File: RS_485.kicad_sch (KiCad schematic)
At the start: 17 parts, among them U6 SP3071EEN-L/TR

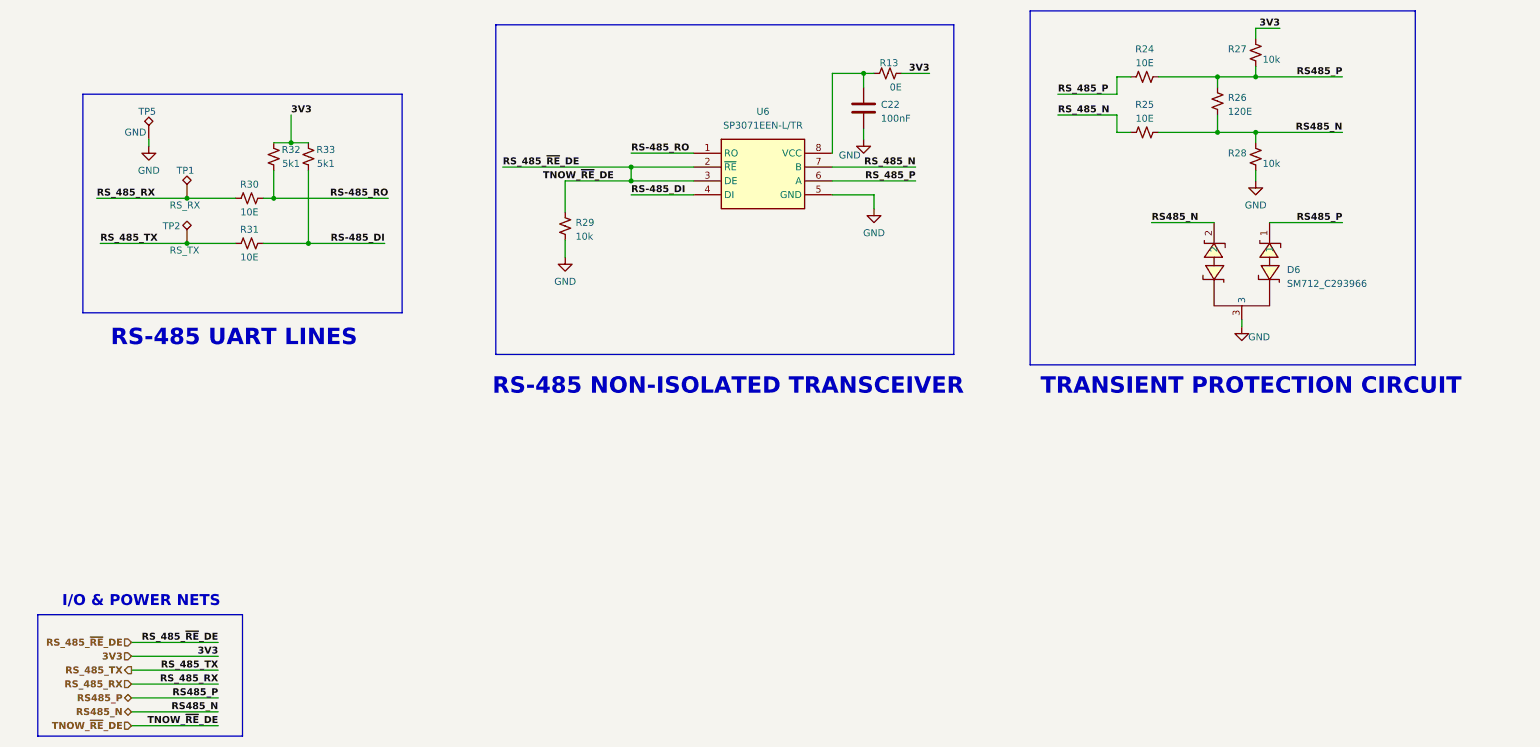
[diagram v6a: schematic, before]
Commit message: Changed GPIO mapping
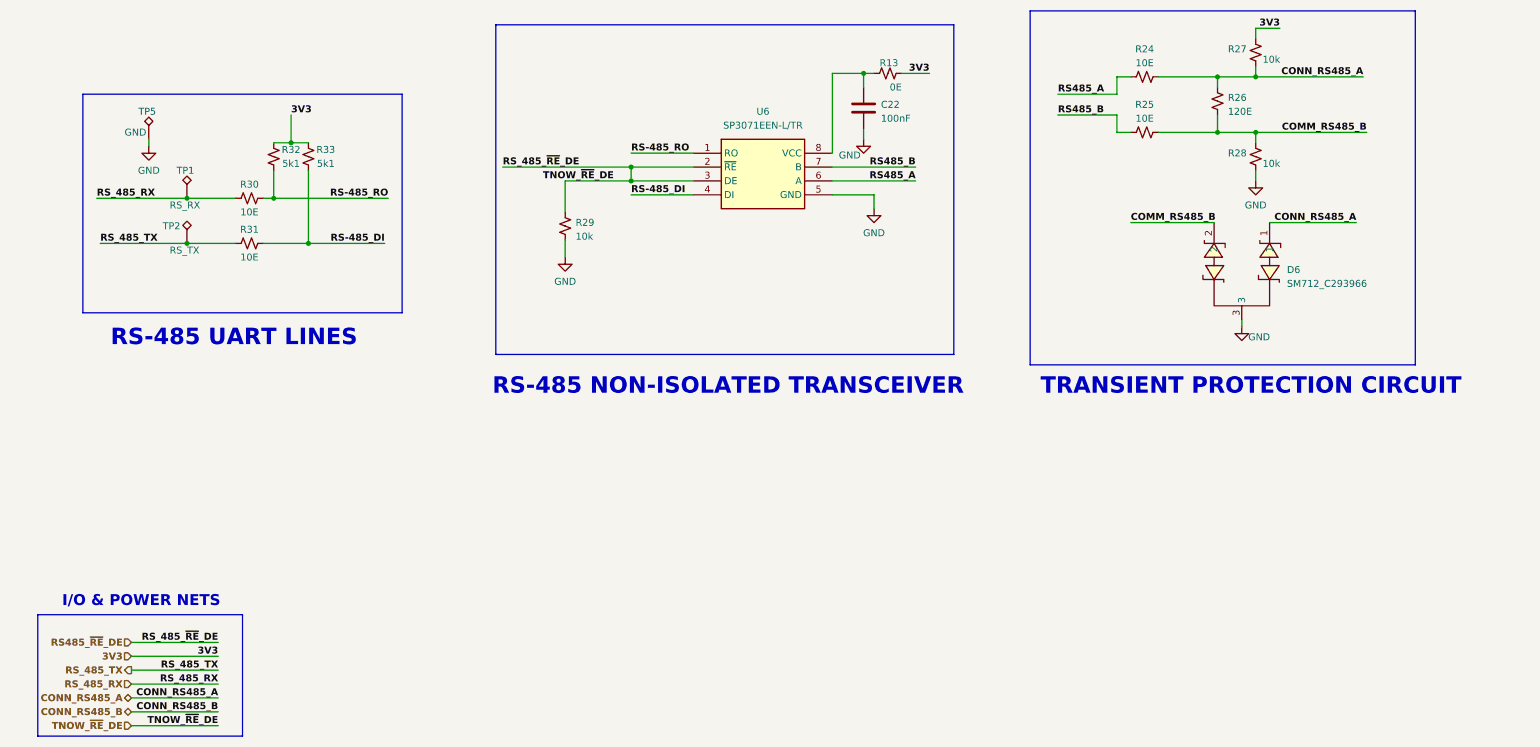
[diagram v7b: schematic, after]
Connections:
- net RS485_N renamed COMM_RS485_B
- net RS485_P renamed CONN_RS485_A
- net RS_485_N renamed RS485_B
- net RS_485_P renamed RS485_A
- net RS_485_~{RE}_DE renamed RS485_~{RE}_DE
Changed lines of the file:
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@@
     (stroke (width 0) (type default))
   )
-  (wire (pts (xy 234.95 97.79) (xy 223.52 97.79))
+  (wire (pts (xy 234.95 97.79) (xy 219.71 97.79))
     (stroke (width 0) (type default))
   )
@@
     (stroke (width 0) (type default))
   )
-  (wire (pts (xy 242.57 81.28) (xy 258.445 81.28))
+  (wire (pts (xy 242.57 81.28) (xy 262.89 81.28))
     (stroke (width 0) (type default))
   )
@@
     (stroke (width 0) (type default))
   )
-  (wire (pts (xy 242.57 71.12) (xy 258.445 71.12))
+  (wire (pts (xy 242.57 71.12) (xy 262.255 71.12))
     (stroke (width 0) (type default))
   )
@@
     (stroke (width 0.5) (type default) (color 0 0 0 1))
   )
-  (wire (pts (xy 258.445 97.79) (xy 245.11 97.79))
+  (wire (pts (xy 260.985 97.79) (xy 245.11 97.79))
     (stroke (width 0) (type default))
   )
@@
     (effects (font (size 3 3) bold (color 255 0 0 1)) (justify left bottom))
   )
-  (label "RS485_P" (at 258.445 97.79 180) (fields_autoplaced)
-    (effects (font (size 1.27 1.27) (thickness 0.254) bold (color 0 0 0 1)) (justify right bottom))
+  (label "RS485_B" (at 206.375 78.105 0) (fields_autoplaced)
+    (effects (font (size 1.27 1.27) bold (color 0 0 255 1)) (justify left bottom))
   )
   (label "3V3" (at 52.705 177.165 180) (fields_autoplaced)
     (effects (font (size 1.27 1.27) (thickness 0.254) bold (color 255 0 0 1)) (justify right bottom))
   )
-  (label "RS485_P" (at 52.705 184.785 180) (fields_autoplaced)
-    (effects (font (size 1.27 1.27) (thickness 0.254) bold (color 0 0 0 1)) (justify right bottom))
-  )
-  (label "RS485_N" (at 258.445 81.28 180) (fields_autoplaced)
+  (label "COMM_RS485_B" (at 262.89 81.28 180) (fields_autoplaced)
     (effects (font (size 1.27 1.27) (thickness 0.254) bold (color 0 0 0 1)) (justify right bottom))
   )
@@
     (effects (font (size 1.27 1.27) (thickness 0.254) bold (color 0 0 255 1)) (justify right bottom))
   )
+  (label "COMM_RS485_B" (at 219.71 97.79 0) (fields_autoplaced)
+    (effects (font (size 1.27 1.27) (thickness 0.254) bold (color 0 0 0 1)) (justify left bottom))
+  )
   (label "RS_485_~{RE}_DE" (at 104.775 87.63 0) (fields_autoplaced)
     (effects (font (size 1.27 1.27) bold (color 0 194 0 1)) (justify left bottom))
   )
-  (label "RS_485_N" (at 180.34 87.63 180) (fields_autoplaced)
+  (label "RS485_B" (at 180.34 87.63 180) (fields_autoplaced)
     (effects (font (size 1.27 1.27) bold (color 0 0 255 1)) (justify right bottom))
   )
@@
     (effects (font (size 1.27 1.27) (thickness 0.254) bold (color 0 0 255 1)) (justify right bottom))
   )
-  (label "RS485_P" (at 258.445 71.12 180) (fields_autoplaced)
+  (label "CONN_RS485_A" (at 262.255 71.12 180) (fields_autoplaced)
+    (effects (font (size 1.27 1.27) (thickness 0.254) bold (color 0 0 0 1)) (justify right bottom))
+  )
+  (label "CONN_RS485_A" (at 260.985 97.79 180) (fields_autoplaced)
     (effects (font (size 1.27 1.27) (thickness 0.254) bold (color 0 0 0 1)) (justify right bottom))
   )
@@
     (effects (font (size 1.27 1.27) bold (color 0 0 255 1)) (justify left bottom))
   )
-  (label "RS485_N" (at 52.705 187.325 180) (fields_autoplaced)
-    (effects (font (size 1.27 1.27) (thickness 0.254) bold (color 0 0 0 1)) (justify right bottom))
-  )
-  (label "RS_485_P" (at 206.375 74.295 0) (fields_autoplaced)
+  (label "RS485_A" (at 206.375 74.295 0) (fields_autoplaced)
     (effects (font (size 1.27 1.27) bold (color 0 0 255 1)) (justify left bottom))
   )
@@
     (effects (font (size 1.27 1.27) (thickness 0.254) bold (color 0 0 255 1)) (justify left bottom))
   )
+  (label "CONN_RS485_A" (at 52.705 184.785 180) (fields_autoplaced)
+    (effects (font (size 1.27 1.27) (thickness 0.254) bold (color 0 0 0 1)) (justify right bottom))
+  )
   (label "TNOW_~{RE}_DE" (at 52.705 189.865 180) (fields_autoplaced)
     (effects (font (size 1.27 1.27) bold (color 0 194 0 1)) (justify right bottom))
@@
     (effects (font (size 1.27 1.27) bold (color 0 0 255 1)) (justify left bottom))
   )
-  (label "RS_485_N" (at 206.375 78.105 0) (fields_autoplaced)
-    (effects (font (size 1.27 1.27) bold (color 0 0 255 1)) (justify left bottom))
-  )
   (label "3V3" (at 66.04 78.105 0) (fields_autoplaced)
     (effects (font (size 1.27 1.27) (thickness 0.254) bold (color 255 0 0 1)) (justify left bottom))
@@
     (effects (font (size 1.27 1.27) bold (color 0 194 0 1)) (justify right bottom))
   )
-  (label "RS_485_P" (at 180.34 90.17 180) (fields_autoplaced)
+  (label "CONN_RS485_B" (at 52.705 187.325 180) (fields_autoplaced)
+    (effects (font (size 1.27 1.27) (thickness 0.254) bold (color 0 0 0 1)) (justify right bottom))
+  )
+  (label "RS485_A" (at 180.34 90.17 180) (fields_autoplaced)
     (effects (font (size 1.27 1.27) bold (color 0 0 255 1)) (justify right bottom))
-  )
-  (label "RS485_N" (at 223.52 97.79 0) (fields_autoplaced)
-    (effects (font (size 1.27 1.27) (thickness 0.254) bold (color 0 0 0 1)) (justify left bottom))
   )
   (hierarchical_label "RS_485_TX" (shape output) (at 36.83 179.705 180) (fields_autoplaced)
     (effects (font (size 1.27 1.27) bold (color 0 0 255 1)) (justify right))
   )
-  (hierarchical_label "RS485_P" (shape bidirectional) (at 36.83 184.785 180) (fields_autoplaced)
+  (hierarchical_label "CONN_RS485_A" (shape bidirectional) (at 36.83 184.785 180) (fields_autoplaced)
     (effects (font (size 1.27 1.27) bold (color 0 0 0 1)) (justify right))
   )
@@
     (effects (font (size 1.27 1.27) bold (color 0 0 255 1)) (justify right))
   )
-  (hierarchical_label "RS_485_~{RE}_DE" (shape input) (at 36.83 174.625 180) (fields_autoplaced)
+  (hierarchical_label "RS485_~{RE}_DE" (shape input) (at 36.83 174.625 180) (fields_autoplaced)
     (effects (font (size 1.27 1.27) bold (color 0 194 0 1)) (justify right))
   )
-  (hierarchical_label "RS485_N" (shape bidirectional) (at 36.83 187.325 180) (fields_autoplaced)
+  (hierarchical_label "CONN_RS485_B" (shape bidirectional) (at 36.83 187.325 180) (fields_autoplaced)
     (effects (font (size 1.27 1.27) bold (color 0 0 0 1)) (justify right))
   )

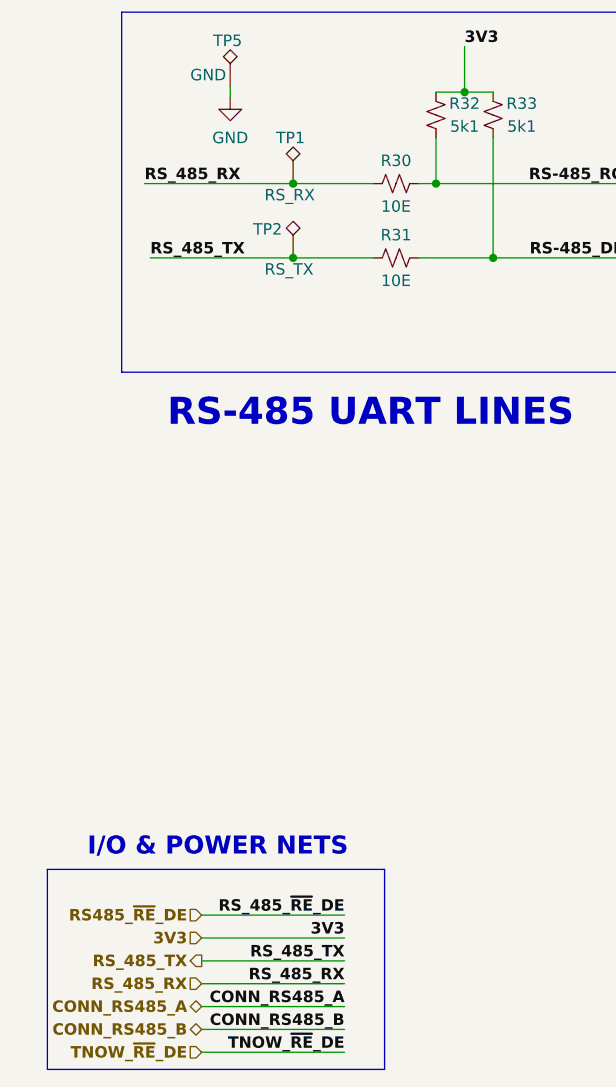
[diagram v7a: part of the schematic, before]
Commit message: Completed routing for all GPIO pins
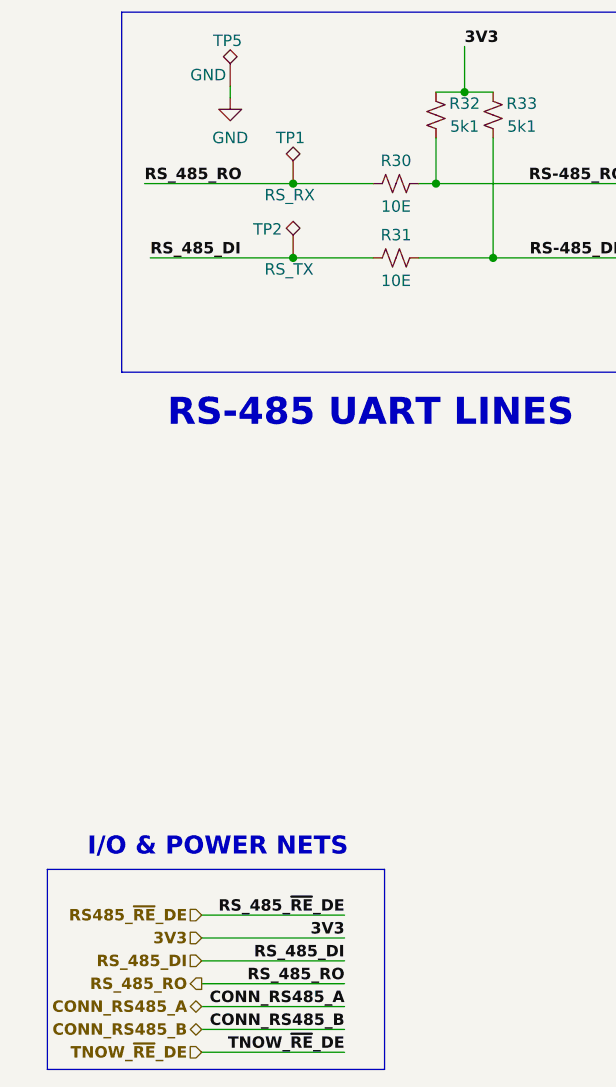
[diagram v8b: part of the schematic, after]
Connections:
- net RS_485_RX renamed RS_485_RO
- net RS_485_TX renamed RS_485_DI
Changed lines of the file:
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@@
     (effects (font (size 1.27 1.27) (thickness 0.254) bold (color 255 0 0 1)) (justify right bottom))
   )
-  (label "RS_485_TX" (at 31.115 101.6 0) (fields_autoplaced)
+  (label "RS_485_DI" (at 31.115 101.6 0) (fields_autoplaced)
     (effects (font (size 1.27 1.27) (thickness 0.254) bold (color 0 0 255 1)) (justify left bottom))
   )
@@
     (effects (font (size 1.27 1.27) bold (color 0 0 255 1)) (justify right bottom))
   )
-  (label "RS_485_RX" (at 52.705 182.245 180) (fields_autoplaced)
+  (label "RS_485_RO" (at 52.705 182.245 180) (fields_autoplaced)
     (effects (font (size 1.27 1.27) (thickness 0.254) bold (color 0 0 255 1)) (justify right bottom))
   )
@@
     (effects (font (size 1.27 1.27) bold (color 0 0 255 1)) (justify right bottom))
   )
-  (label "RS_485_TX" (at 52.705 179.705 180) (fields_autoplaced)
+  (label "RS_485_DI" (at 52.705 179.705 180) (fields_autoplaced)
     (effects (font (size 1.27 1.27) (thickness 0.254) bold (color 0 0 255 1)) (justify right bottom))
   )
@@
     (effects (font (size 1.27 1.27) bold (color 0 0 255 1)) (justify left bottom))
   )
-  (label "RS_485_RX" (at 30.48 93.345 0) (fields_autoplaced)
+  (label "RS_485_RO" (at 30.48 93.345 0) (fields_autoplaced)
     (effects (font (size 1.27 1.27) (thickness 0.254) bold (color 0 0 255 1)) (justify left bottom))
   )
@@
     (effects (font (size 1.27 1.27) bold (color 0 0 255 1)) (justify right bottom))
   )
-  (hierarchical_label "RS_485_TX" (shape output) (at 36.83 179.705 180) (fields_autoplaced)
+  (hierarchical_label "RS_485_DI" (shape input) (at 36.83 179.705 180) (fields_autoplaced)
     (effects (font (size 1.27 1.27) bold (color 0 0 255 1)) (justify right))
   )
@@
     (effects (font (size 1.27 1.27) (thickness 0.254) bold (color 255 0 0 1)) (justify right))
   )
-  (hierarchical_label "RS_485_RX" (shape input) (at 36.83 182.245 180) (fields_autoplaced)
+  (hierarchical_label "RS_485_RO" (shape output) (at 36.83 182.245 180) (fields_autoplaced)
     (effects (font (size 1.27 1.27) bold (color 0 0 255 1)) (justify right))
   )
